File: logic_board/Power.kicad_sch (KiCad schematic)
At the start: 16 parts, among them J3 USB_C_Receptacle_USB2.0_16P, J5 Battery, SW5 SW_SPDT, U3 BQ25185DLHR, U4 AP2112K-3.3, U5 USBLC6-2SC6

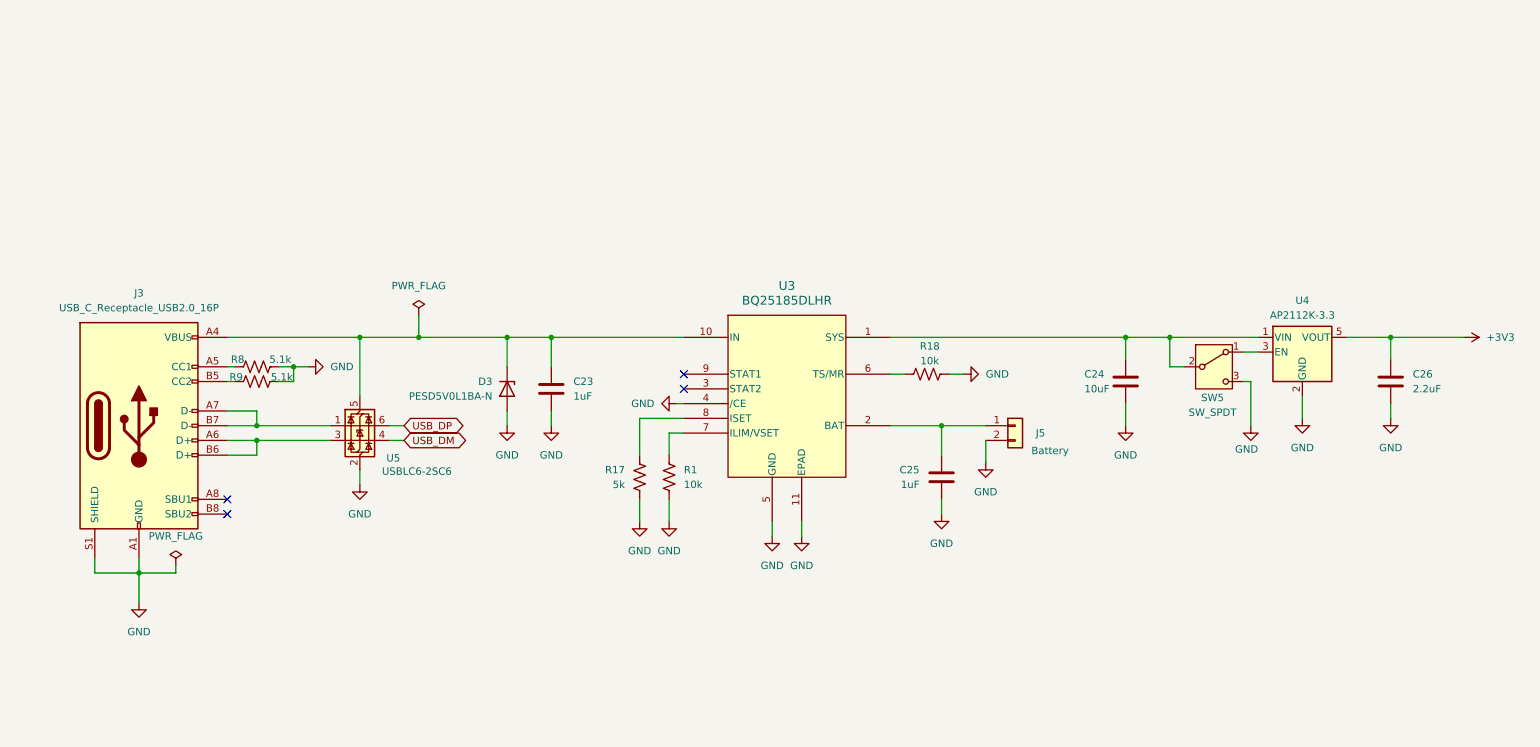
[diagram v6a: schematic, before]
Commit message: Change how charge management is handled
The LDO (and microcontroller) are now enabled even if the power switch is off when the device is charging.
Added a bi-color LED to indicate charging status (driven by microcontroller)
Charge status now routed to the microcontroller, as well as power switch status.

(Note this would also allow data transfer to the microcontroller when plugged in when the power switch is off, which is probably desirable).
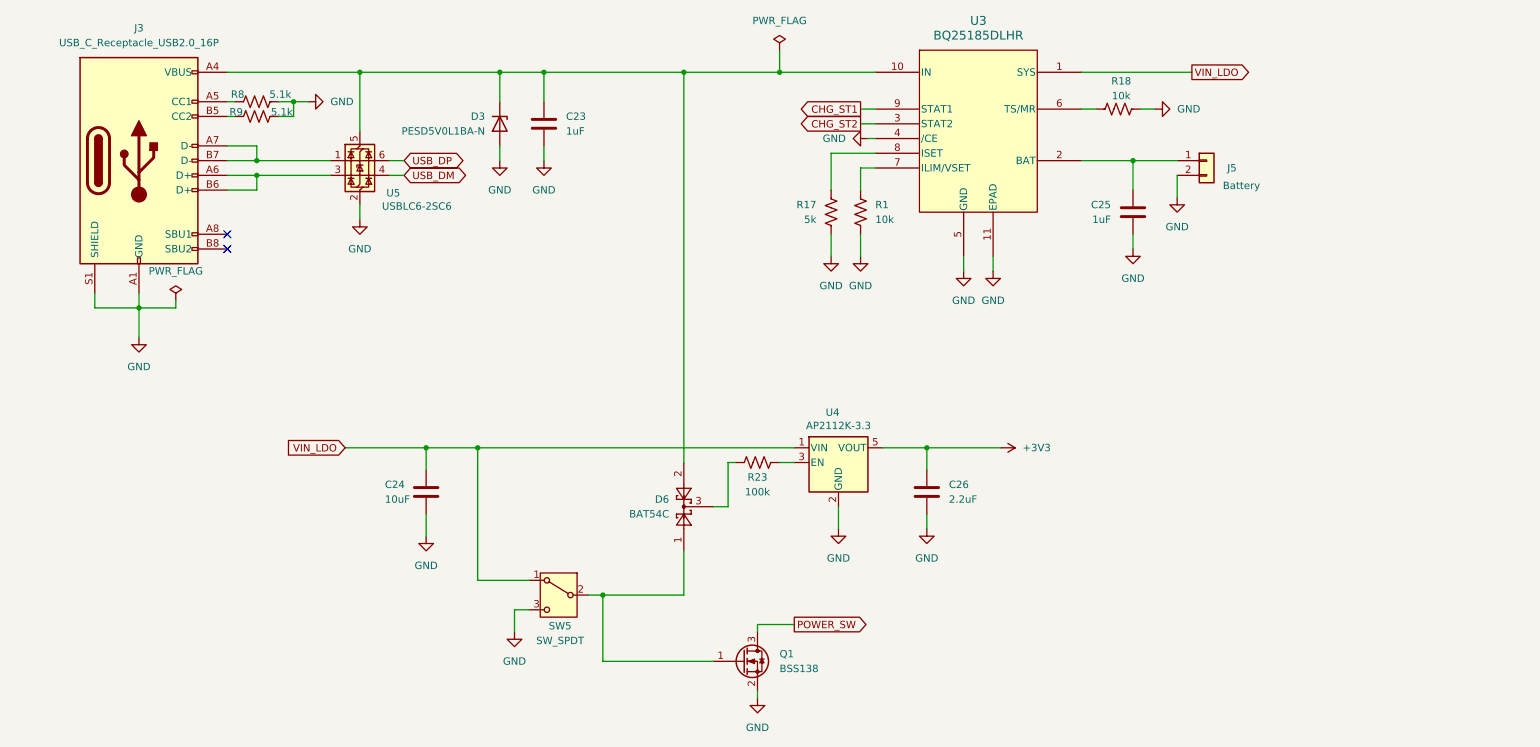
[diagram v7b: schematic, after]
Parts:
- added D6: BAT54C, Package_TO_SOT_SMD:SOT-23, symbol Diode:BAT54C
- added Q1: BSS138, Package_TO_SOT_SMD:SOT-23, symbol Transistor_FET:BSS138
- added R23: 100k, Resistor_SMD:R_0603_1608Metric, symbol Device:R_US
- R1, R18: footprint (none) -> Resistor_SMD:R_0603_1608Metric
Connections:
- net GND: now also Q1.2 (S)
- net VIN_LDO: now reaches C24.1, U3.1 (SYS), U4.1 (VIN)
- net VIN_LDO: now also SW5.1 (A); no longer SW5.2 (B)
- net at U4.3 (EN): now also R23.2; no longer SW5.1 (A)
- net at C23.1, D3.1 (K), J3.A4 (VBUS)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: now also D6.2
- net CHG_ST2: now reaches U3.3 (STAT2)
- net CHG_ST1: now reaches U3.9 (STAT1)
- new net: D6.3, R23.1
- new net: D6.1, Q1.1 (G), SW5.2 (B)
- new net POWER_SW: Q1.3 (D)
- no-connect marks 4 -> 2
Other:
- moved on the sheet: C23, C24, C25, C26, D3, J3, J5, R1, R17, R18, R8, R9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

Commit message: More component placement tweaking, mostly around audio section.
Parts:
- J5: now left out of the parts list
- SW5: LCSC Part Number (none) -> C125040; LCSC part number C125040 -> (none); now left out of the parts list
- U3: LCSC Part Number (none) -> C19725033
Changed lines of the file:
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@@
+			)
+		)
+		(property "LCSC part number" ""
+			(at 57.15 44.45 90)
+			(effects
+				(font
+					(size 1.27 1.27)
+				)
+				(hide yes)
 			)
 		)
@@
 			)
 		)
+		(property "LCSC part number" ""
+			(at 143.51 104.14 90)
+			(effects
+				(font
+					(size 1.27 1.27)
+				)
+				(hide yes)
+			)
+		)
 		(pin "1"
 		)
@@
 			)
 		)
+		(property "LCSC part number" ""
+			(at 157.48 104.14 0)
+			(effects
+				(font
+					(size 1.27 1.27)
+				)
+				(hide yes)
+			)
+		)
 		(pin "2"
 		)
@@
 			)
 		)
+		(property "LCSC part number" ""
+			(at 172.72 109.22 0)
+			(effects
+				(font
+					(size 1.27 1.27)
+				)
+				(hide yes)
+			)
+		)
 		(pin "2"
 		)
@@
 			)
 		)
+		(property "LCSC part number" ""
+			(at 130.81 111.76 90)
+			(effects
+				(font
+					(size 1.27 1.27)
+				)
+				(hide yes)
+			)
+		)
 		(pin "1"
 		)
@@
 			)
 		)
+		(property "LCSC part number" ""
+			(at 140.97 138.43 0)
+			(effects
+				(font
+					(size 1.27 1.27)
+				)
+				(hide yes)
+			)
+		)
 		(pin "3"
 		)
@@
 			)
 		)
+		(property "LCSC part number" ""
+			(at 161.29 60.96 0)
+			(effects
+				(font
+					(size 1.27 1.27)
+				)
+				(hide yes)
+			)
+		)
 		(pin "1"
 		)
@@
 			)
 		)
+		(property "LCSC Part Number" "C19725033"
+			(at 181.61 45.72 0)
+			(effects
+				(font
+					(size 1.27 1.27)
+				)
+				(hide yes)
+			)
+		)
+		(property "LCSC part number" ""
+			(at 181.61 45.72 0)
+			(effects
+				(font
+					(size 1.27 1.27)
+				)
+				(hide yes)
+			)
+		)
 		(pin "3"
 		)
@@
 			)
 		)
+		(property "LCSC part number" ""
+			(at 205.74 43.18 90)
+			(effects
+				(font
+					(size 1.27 1.27)
+				)
+				(hide yes)
+			)
+		)
 		(pin "1"
 		)
@@
 			)
 		)
+		(property "LCSC part number" ""
+			(at 156.21 60.96 0)
+			(effects
+				(font
+					(size 1.27 1.27)
+				)
+				(hide yes)
+			)
+		)
 		(pin "1"
 		)
@@
 			)
 		)
+		(property "LCSC part number" ""
+			(at 208.28 60.96 0)
+			(effects
+				(font
+					(size 1.27 1.27)
+				)
+				(hide yes)
+			)
+		)
 		(pin "1"
 		)
@@
 		(unit 1)
 		(exclude_from_sim no)
-		(in_bom yes)
+		(in_bom no)
 		(on_board yes)
 		(dnp no)
@@
 			)
 		)
+		(property "LCSC part number" ""
+			(at 220.98 52.07 0)
+			(effects
+				(font
+					(size 1.27 1.27)
+				)
+				(hide yes)
+			)
+		)
 		(pin "2"
 		)
@@
 			)
 		)
+		(property "LCSC part number" ""
+			(at 57.15 41.91 90)
+			(effects
+				(font
+					(size 1.27 1.27)
+				)
+				(hide yes)
+			)
+		)
 		(pin "2"
 		)
@@
 			)
 		)
+		(property "LCSC part number" ""
+			(at 86.36 109.22 0)
+			(effects
+				(font
+					(size 1.27 1.27)
+				)
+				(hide yes)
+			)
+		)
 		(pin "1"
 		)
@@
 			)
 		)
+		(property "LCSC part number" ""
+			(at 74.93 52.07 0)
+			(effects
+				(font
+					(size 1.27 1.27)
+				)
+				(hide yes)
+			)
+		)
 		(pin "3"
 		)
@@
 			)
 		)
+		(property "LCSC part number" ""
+			(at 106.68 45.72 0)
+			(effects
+				(font
+					(size 1.27 1.27)
+				)
+				(hide yes)
+			)
+		)
 		(pin "1"
 		)
@@
 		)
 		(property "LCSC Part Number" "C165948"
+			(at 36.83 52.07 0)
+			(effects
+				(font
+					(size 1.27 1.27)
+				)
+				(hide yes)
+			)
+		)
+		(property "LCSC part number" ""
 			(at 36.83 52.07 0)
 			(effects
@@
 		(unit 1)
 		(exclude_from_sim no)
-		(in_bom yes)
+		(in_bom no)
 		(on_board yes)
 		(dnp no)
@@
 			)
 		)
-		(property "LCSC part number" "C125040"
+		(property "LCSC Part Number" "C125040"
+			(at 109.22 127 0)
+			(effects
+				(font
+					(size 1.27 1.27)
+				)
+				(hide yes)
+			)
+		)
+		(property "LCSC part number" ""
 			(at 109.22 127 0)
 			(effects
@@
 			(at 99.06 45.72 90)
 			(effects
+				(font
+					(size 1.27 1.27)
+				)
+				(hide yes)
+			)
+		)
+		(property "LCSC part number" ""
+			(at 99.06 45.72 90)
+			(effects
